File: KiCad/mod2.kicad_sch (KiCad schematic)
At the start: 44 parts, among them M3 Fan_4pin, M4 Fan_4pin

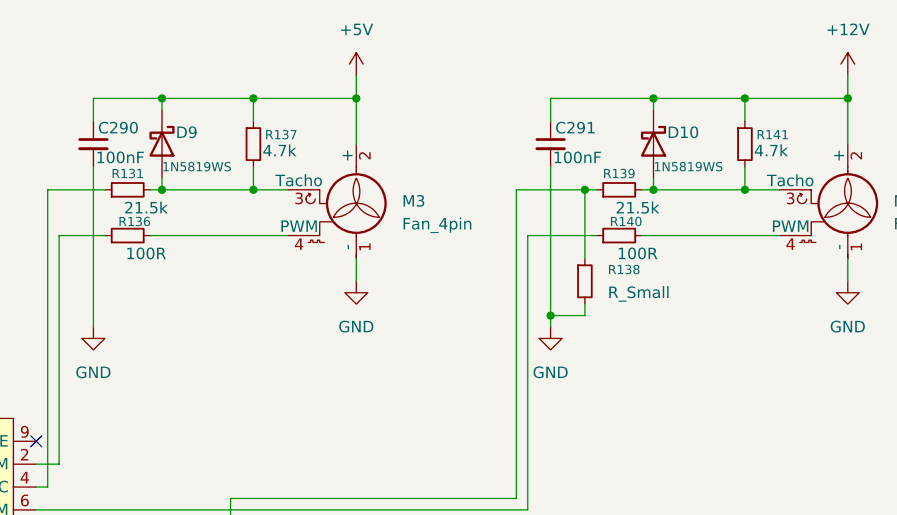
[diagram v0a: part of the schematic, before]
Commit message: Fix some diodes and resistors
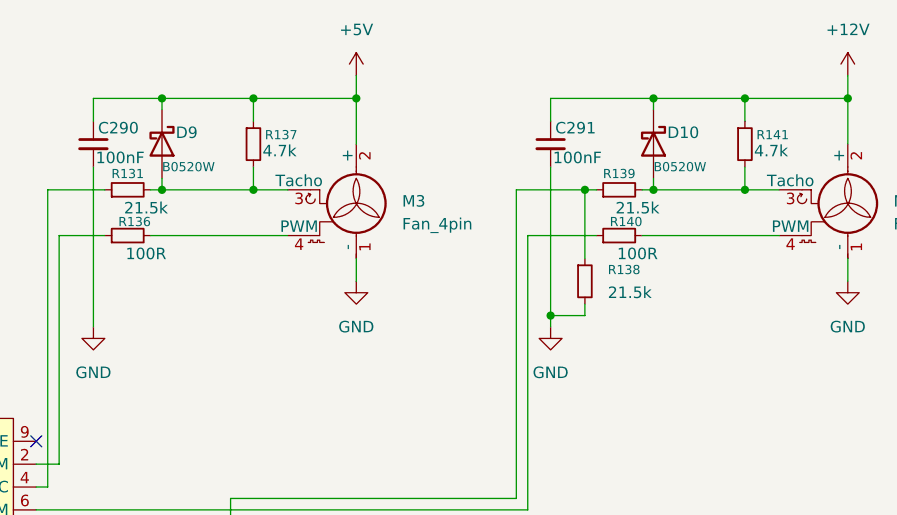
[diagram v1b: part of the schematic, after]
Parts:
- D10, D9: value 1N5819WS -> B0520W
- R138: value R_Small -> 21.5k
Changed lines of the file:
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@@
 			)
 		)
-		(property "Value" "1N5819WS"
+		(property "Value" "B0520W"
 			(at 341.63 59.69 90)
 			(effects
@@
 			)
 		)
-		(property "Value" "1N5819WS"
+		(property "Value" "B0520W"
 			(at 396.24 59.69 90)
 			(effects
@@
 			)
 		)
-		(property "Value" "R_Small"
+		(property "Value" "21.5k"
 			(at 391.16 73.6599 0)
 			(effects

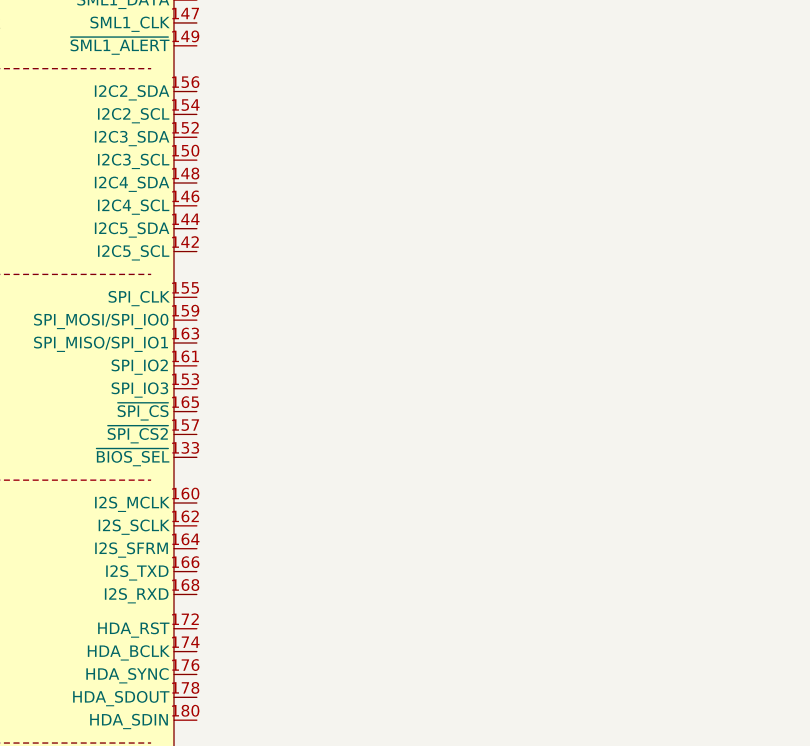
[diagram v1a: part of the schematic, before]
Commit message: Add external BIOS flash
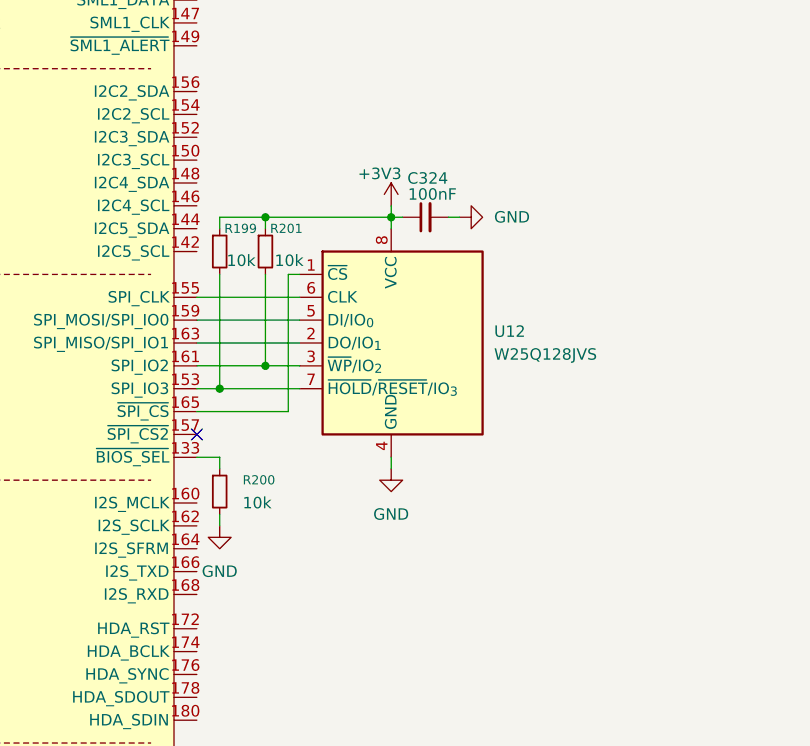
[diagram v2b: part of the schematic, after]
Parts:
- added C324: 100nF, symbol Device:C_Small
- added R199, R200, R201: 10k, symbol Device:R_Small
- added U12: W25Q128JVS, Package_SO:SOIC-8_5.3x5.3mm_P1.27mm, symbol Memory_Flash:W25Q128JVS
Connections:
- net +3V3: now also C324.1, R199.1, R201.1, U12.8 (VCC)
- net GND: now also C324.2, R200.2, U12.4 (GND)
- net at A2.133 (~{BIOS_SEL}): now also R200.1
- net at A2.153 (SPI_IO3): now also R199.2, U12.7 (~{HOLD}/~{RESET}/IO_{3})
- net at A2.155 (SPI_CLK): now also U12.6 (CLK)
- net at A2.159 (SPI_MOSI/SPI_IO0): now also U12.5 (DI/IO_{0})
- net at A2.161 (SPI_IO2): now also R201.2, U12.3 (~{WP}/IO_{2})
- net at A2.163 (SPI_MISO/SPI_IO1): now also U12.2 (DO/IO_{1})
- net at A2.165 (~{SPI_CS}): now also U12.1 (~{CS})
- no-connect marks 5 -> 6

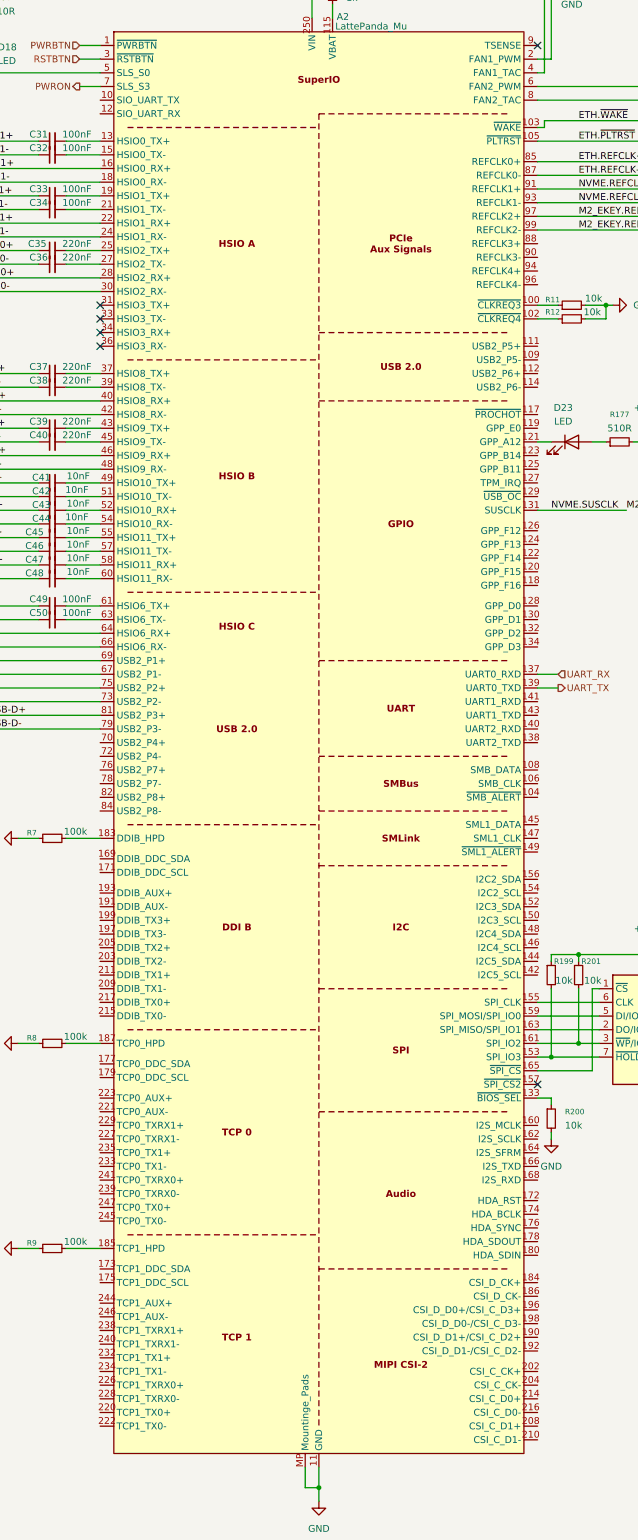
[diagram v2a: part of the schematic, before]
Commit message: Remove 0.95V Power Supply, Replace 3.3V Standby Power Supply
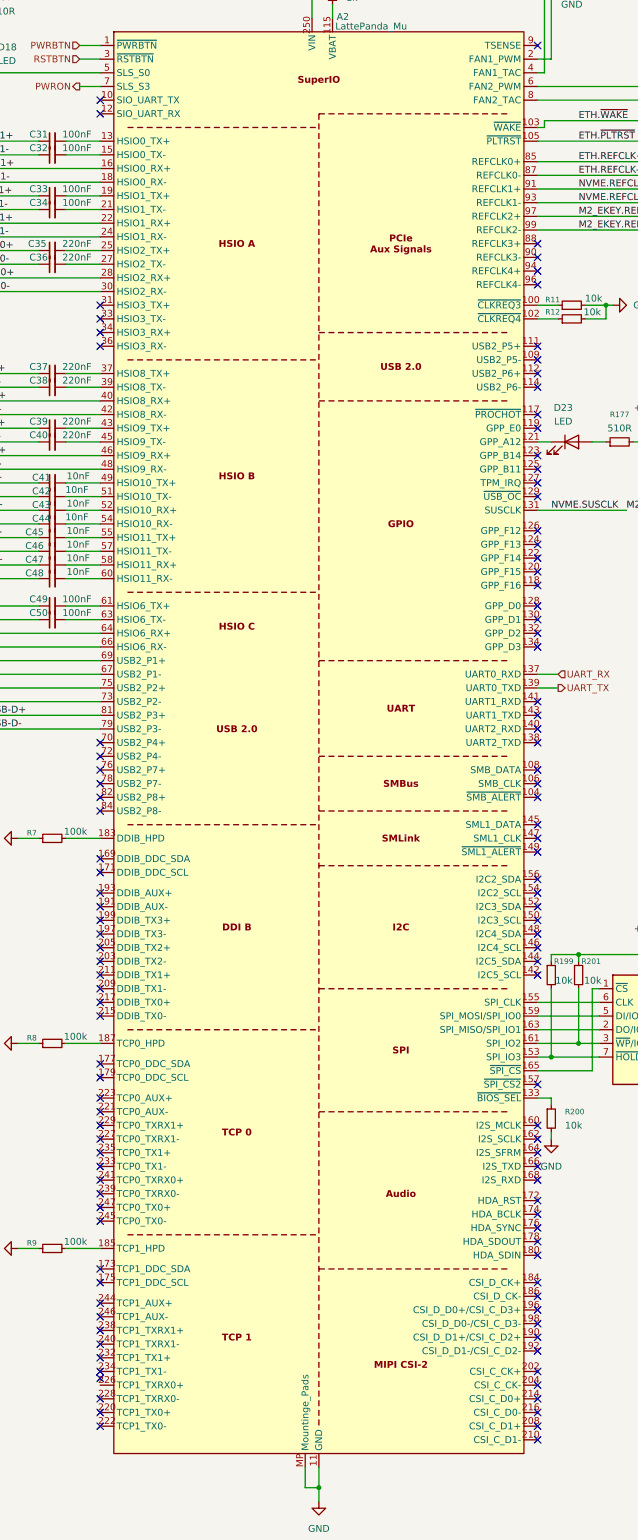
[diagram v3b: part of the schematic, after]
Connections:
- no-connect marks 6 -> 113

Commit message: Work though ERC errors
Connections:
- net ETH.SMBDAT: now reaches A2.145 (SML1_DATA)
- net ETH.SMBCLK: now reaches A2.147 (SML1_CLK)
- no-connect marks 113 -> 111
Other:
- moved on the sheet: R10
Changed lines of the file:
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@@
 	)
 	(junction
+		(at 289.56 82.55)
+		(diameter 0)
+		(color 0 0 0 0)
+	)
+	(junction
 		(at 417.83 52.07)
 		(diameter 0)
@@
 	)
 	(no_connect
-		(at 327.66 234.95)
-	)
-	(no_connect
 		(at 327.66 332.74)
 	)
@@
 	)
 	(no_connect
-		(at 327.66 237.49)
-	)
-	(no_connect
 		(at 246.38 326.39)
 	)
@@
 	)
 	(no_connect
-		(at 246.38 337.82)
+		(at 246.38 339.09)
 	)
 	(no_connect
@@
 	)
 	(bus_entry
+		(at 344.17 234.95)
+		(size -2.54 2.54)
+		(stroke
+			(width 0)
+			(type default)
+		)
+	)
+	(bus_entry
+		(at 344.17 232.41)
+		(size -2.54 2.54)
+		(stroke
+			(width 0)
+			(type default)
+		)
+	)
+	(bus_entry
 		(at 213.36 115.57)
 		(size 2.54 2.54)
@@
 	(wire
 		(pts
+			(xy 295.91 80.01) (xy 295.91 82.55)
+		)
+		(stroke
+			(width 0)
+			(type default)
+		)
+	)
+	(wire
+		(pts
 			(xy 382.27 97.79) (xy 382.27 67.31)
 		)
@@
 		)
 	)
+	(bus
+		(pts
+			(xy 344.17 232.41) (xy 344.17 234.95)
+		)
+		(stroke
+			(width 0)
+			(type default)
+		)
+	)
 	(wire
 		(pts
@@
 	(wire
 		(pts
+			(xy 327.66 234.95) (xy 341.63 234.95)
+		)
+		(stroke
+			(width 0)
+			(type default)
+		)
+	)
+	(wire
+		(pts
 			(xy 240.03 196.85) (xy 246.38 196.85)
 		)
@@
 		)
 	)
+	(wire
+		(pts
+			(xy 295.91 82.55) (xy 289.56 82.55)
+		)
+		(stroke
+			(width 0)
+			(type default)
+		)
+	)
 	(bus
 		(pts
@@
 	(wire
 		(pts
+			(xy 327.66 237.49) (xy 341.63 237.49)
+		)
+		(stroke
+			(width 0)
+			(type default)
+		)
+	)
+	(wire
+		(pts
 			(xy 215.9 130.81) (xy 234.95 130.81)
 		)
@@
 	(wire
 		(pts
+			(xy 289.56 82.55) (xy 289.56 85.09)
+		)
+		(stroke
+			(width 0)
+			(type default)
+		)
+	)
+	(wire
+		(pts
 			(xy 240.03 163.83) (xy 246.38 163.83)
 		)
@@
 	(wire
 		(pts
-			(xy 289.56 74.93) (xy 289.56 77.47)
+			(xy 289.56 74.93) (xy 289.56 76.2)
 		)
 		(stroke
@@
 		)
 	)
+	(bus
+		(pts
+			(xy 344.17 231.14) (xy 344.17 232.41)
+		)
+		(stroke
+			(width 0)
+			(type default)
+		)
+	)
 	(wire
 		(pts
@@
 	(wire
 		(pts
-			(xy 289.56 82.55) (xy 289.56 85.09)
+			(xy 289.56 81.28) (xy 289.56 82.55)
 		)
 		(stroke
@@
 		)
 	)
+	(label "ETH.SMBCLK"
+		(at 328.93 237.49 0)
+		(effects
+			(font
+				(size 1.27 1.27)
+			)
+			(justify left bottom)
+		)
+	)
 	(label "ETH.REFCLK-"
 		(at 335.28 114.3 0)
@@
 		)
 	)
+	(label "ETH{PCIE}"
+		(at 344.17 231.14 0)
+		(effects
+			(font
+				(size 1.27 1.27)
+			)
+			(justify left bottom)
+		)
+	)
 	(label "SATA2.Tx+"
 		(at 218.44 181.61 0)
@@
 		)
 	)
+	(label "ETH.SMBDAT"
+		(at 328.93 234.95 0)
+		(effects
+			(font
+				(size 1.27 1.27)
+			)
+			(justify left bottom)
+		)
+	)
 	(label "NVME.SUSCLK"
 		(at 330.2 176.53 0)
@@
 	(symbol
 		(lib_id "Device:R_Small")
-		(at 289.56 80.01 0)
+		(at 289.56 78.74 0)
 		(unit 1)
 		(exclude_from_sim no)
@@
 		(fields_autoplaced yes)
 		(property "Reference" "R10"
-			(at 292.1 78.7399 0)
+			(at 292.1 77.4699 0)
 			(effects
 				(font
@@
 		)
 		(property "Value" "1k"
-			(at 292.1 81.2799 0)
+			(at 292.1 80.0099 0)
 			(effects
 				(font
@@
 		)
 		(property "Footprint" ""
-			(at 289.56 80.01 0)
+			(at 289.56 78.74 0)
 			(effects
 				(font
@@
 		)
 		(property "Datasheet" "~"
-			(at 289.56 80.01 0)
+			(at 289.56 78.74 0)
 			(effects
 				(font
@@
 		)
 		(property "Description" "Resistor, small symbol"
-			(at 289.56 80.01 0)
+			(at 289.56 78.74 0)
 			(effects
 				(font
@@
 					(unit 1)
 				)
+			)
+		)
+	)
+	(symbol
+		(lib_id "power:PWR_FLAG")
+		(at 295.91 80.01 0)
+		(unit 1)
+		(exclude_from_sim no)
+		(in_bom yes)
+		(on_board yes)
+		(dnp no)
+		(fields_autoplaced yes)
+		(property "Reference" "#FLG012"
+			(at 295.91 78.105 0)
+			(effects
+				(font
+					(size 1.27 1.27)
+				)
+				(hide yes)
+			)
+		)
+		(property "Value" "PWR_FLAG"
+			(at 295.91 74.93 0)
+			(effects
+				(font
+					(size 1.27 1.27)
+				)
+			)
+		)
+		(property "Footprint" ""
+			(at 295.91 80.01 0)
+			(effects
+				(font
+					(size 1.27 1.27)
+				)
+				(hide yes)
+			)
+		)
+		(property "Datasheet" "~"
+			(at 295.91 80.01 0)
+			(effects
+				(font
+					(size 1.27 1.27)
+				)
+				(hide yes)
+			)
+		)
+		(property "Description" "Special symbol for telling ERC where power comes from"
+			(at 295.91 80.01 0)
+			(effects
+				(font
+					(size 1.27 1.27)
+				)
+				(hide yes)
+			)
+		)
+		(pin "1"
+		)
+		(instances
+			(project "LattePandaMuCluster"
+				(path "/49abeb3a-c598-45a3-ba6b-595eb04f17a8/22b2f1a4-29b4-42ae-b9cf-15fe0758064e"
+					(reference "#FLG012")
+					(unit 1)
+				)

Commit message: Re-annotate components
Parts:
- C52: renamed from C49; value 100nF -> 220nF
- C53: renamed from C50; value 100nF -> 220nF
- renumbered C31 to C34, C32 to C35, C33 to C36, C34 to C37, C35 to C38, C36 to C39, C37 to C40, C38 to C41, C39 to C42, C40 to C43, C41 to C44, C42 to C45, C43 to C46, C44 to C47, C45 to C48, C46 to C49, C47 to C50, C48 to C51, C290 to C54, C324 to C55, C291 to C56, D18 to D5, D23 to D6, D9 to D7, D10 to D8, R164 to R27, R7 to R28, R8 to R29, R9 to R30, R10 to R31, R199 to R32, R200 to R33, R11 to R34, R12 to R35, R201 to R36, R131 to R37, R136 to R38, R177 to R39, R137 to R40, R138 to R41, R139 to R42, R140 to R43, R141 to R44, U12 to U2

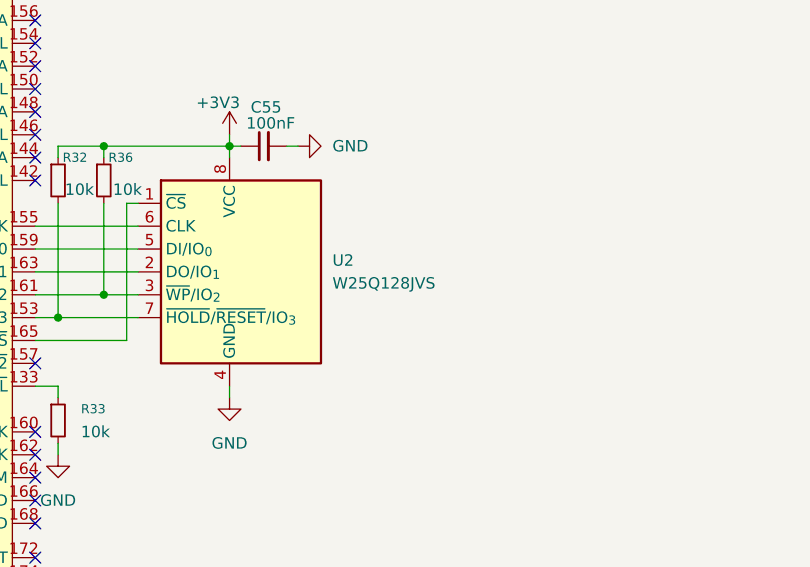
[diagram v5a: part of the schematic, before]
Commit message: Add TVS diodes for ESD protection
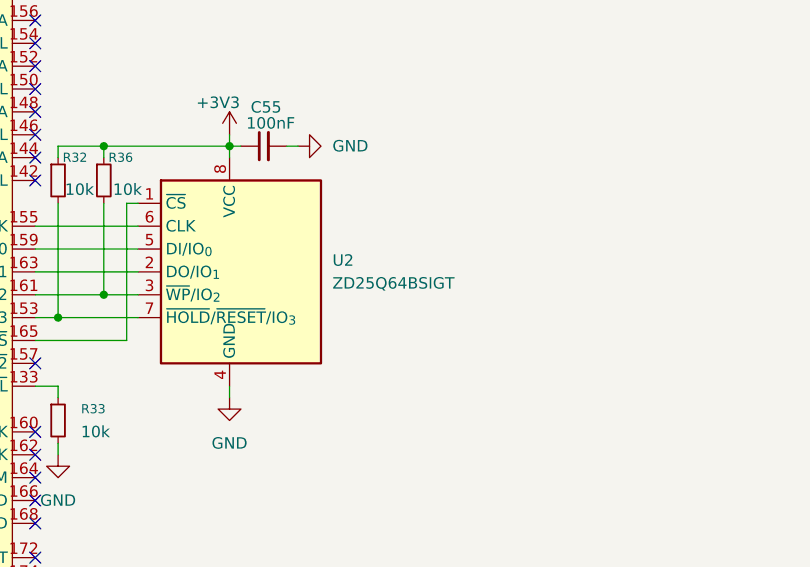
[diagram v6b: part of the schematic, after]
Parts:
- U2: value W25Q128JVS -> ZD25Q64BSIGT
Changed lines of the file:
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@@
 			)
 		)
-		(property "Value" "W25Q128JVS"
+		(property "Value" "ZD25Q64BSIGT"
 			(at 360.68 274.3199 0)
 			(effects

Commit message: Add more footprints
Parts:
- A2: footprint Module_LattePanda:LattePanda_Module_H8.0mm_Horizontal -> 124B-150A02:ATTEND_124B-150A02
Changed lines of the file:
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@@
 			)
 		)
-		(property "Footprint" "Module_LattePanda:LattePanda_Module_H8.0mm_Horizontal"
+		(property "Footprint" "124B-150A02:ATTEND_124B-150A02"
 			(at 287.02 209.55 0)
 			(effects

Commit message: Add more footprints
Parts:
- C34, C35, C36, C37, C38, C39, C40, C41, C42, C43, C44, C45, C46, C47, C48, C49, C50, C51, C52, C53, C54, C55, C56: footprint (none) -> Capacitor_SMD:C_0603_1608Metric
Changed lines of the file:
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@@
 			)
 		)
-		(property "Footprint" ""
+		(property "Footprint" "Capacitor_SMD:C_0603_1608Metric"
 			(at 237.49 181.61 0)
 			(effects
@@
 			)
 		)
-		(property "Footprint" ""
+		(property "Footprint" "Capacitor_SMD:C_0603_1608Metric"
 			(at 237.49 163.83 0)
 			(effects
@@
 			)
 		)
-		(property "Footprint" ""
+		(property "Footprint" "Capacitor_SMD:C_0603_1608Metric"
 			(at 237.49 196.85 0)
 			(effects
@@
 			)
 		)
-		(property "Footprint" ""
+		(property "Footprint" "Capacitor_SMD:C_0603_1608Metric"
 			(at 237.49 176.53 0)
 			(effects
@@
 			)
 		)
-		(property "Footprint" ""
+		(property "Footprint" "Capacitor_SMD:C_0603_1608Metric"
 			(at 353.06 259.08 0)
 			(effects
@@
 			)
 		)
-		(property "Footprint" ""
+		(property "Footprint" "Capacitor_SMD:C_0603_1608Metric"
 			(at 237.49 120.65 0)
 			(effects
@@
 			)
 		)
-		(property "Footprint" ""
+		(property "Footprint" "Capacitor_SMD:C_0603_1608Metric"
 			(at 237.49 194.31 0)
 			(effects
@@
 			)
 		)
-		(property "Footprint" ""
+		(property "Footprint" "Capacitor_SMD:C_0603_1608Metric"
 			(at 237.49 128.27 0)
 			(effects
@@
 			)
 		)
-		(property "Footprint" ""
+		(property "Footprint" "Capacitor_SMD:C_0603_1608Metric"
 			(at 237.49 189.23 0)
 			(effects
@@
 			)
 		)
-		(property "Footprint" ""
+		(property "Footprint" "Capacitor_SMD:C_0603_1608Metric"
 			(at 237.49 179.07 0)
 			(effects
@@
 			)
 		)
-		(property "Footprint" ""
+		(property "Footprint" "Capacitor_SMD:C_0603_1608Metric"
 			(at 237.49 173.99 0)
 			(effects
@@
 			)
 		)
-		(property "Footprint" ""
+		(property "Footprint" "Capacitor_SMD:C_0603_1608Metric"
 			(at 384.81 57.15 0)
 			(effects
@@
 			)
 		)
-		(property "Footprint" ""
+		(property "Footprint" "Capacitor_SMD:C_0603_1608Metric"
 			(at 237.49 107.95 0)
 			(effects
@@
 			)
 		)
-		(property "Footprint" ""
+		(property "Footprint" "Capacitor_SMD:C_0603_1608Metric"
 			(at 237.49 171.45 0)
 			(effects
@@
 			)
 		)
-		(property "Footprint" ""
+		(property "Footprint" "Capacitor_SMD:C_0603_1608Metric"
 			(at 237.49 130.81 0)
 			(effects
@@
 			)
 		)
-		(property "Footprint" ""
+		(property "Footprint" "Capacitor_SMD:C_0603_1608Metric"
 			(at 237.49 161.29 0)
 			(effects
@@
 			)
 		)
-		(property "Footprint" ""
+		(property "Footprint" "Capacitor_SMD:C_0603_1608Metric"
 			(at 237.49 184.15 0)
 			(effects
@@
 			)
 		)
-		(property "Footprint" ""
+		(property "Footprint" "Capacitor_SMD:C_0603_1608Metric"
 			(at 334.01 57.15 0)
 			(effects
@@
 			)
 		)
-		(property "Footprint" ""
+		(property "Footprint" "Capacitor_SMD:C_0603_1608Metric"
 			(at 237.49 151.13 0)
 			(effects
@@
 			)
 		)
-		(property "Footprint" ""
+		(property "Footprint" "Capacitor_SMD:C_0603_1608Metric"
 			(at 237.49 153.67 0)
 			(effects
@@
 			)
 		)
-		(property "Footprint" ""
+		(property "Footprint" "Capacitor_SMD:C_0603_1608Metric"
 			(at 237.49 186.69 0)
 			(effects
@@
 			)
 		)
-		(property "Footprint" ""
+		(property "Footprint" "Capacitor_SMD:C_0603_1608Metric"
 			(at 237.49 118.11 0)
 			(effects
@@
 			)
 		)
-		(property "Footprint" ""
+		(property "Footprint" "Capacitor_SMD:C_0603_1608Metric"
 			(at 237.49 110.49 0)
 			(effects
